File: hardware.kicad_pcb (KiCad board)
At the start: 2 copper layers, 25 x 31 mm, 11 parts, among them J2 MDT320B03001, P1 USB_C_Plug, U4 CH340C

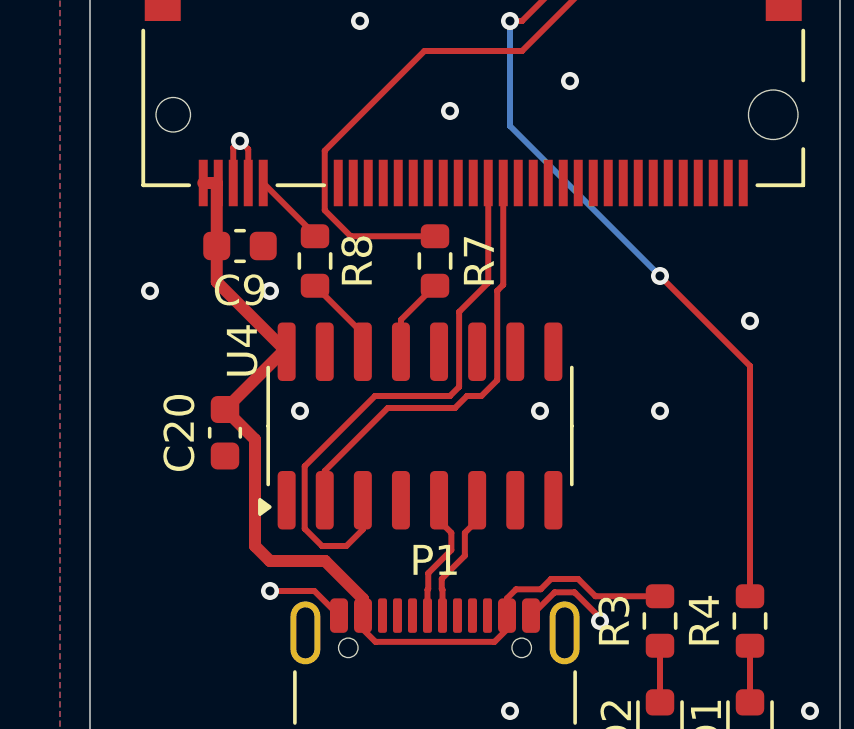
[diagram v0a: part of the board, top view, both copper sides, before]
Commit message: switch uart wiring
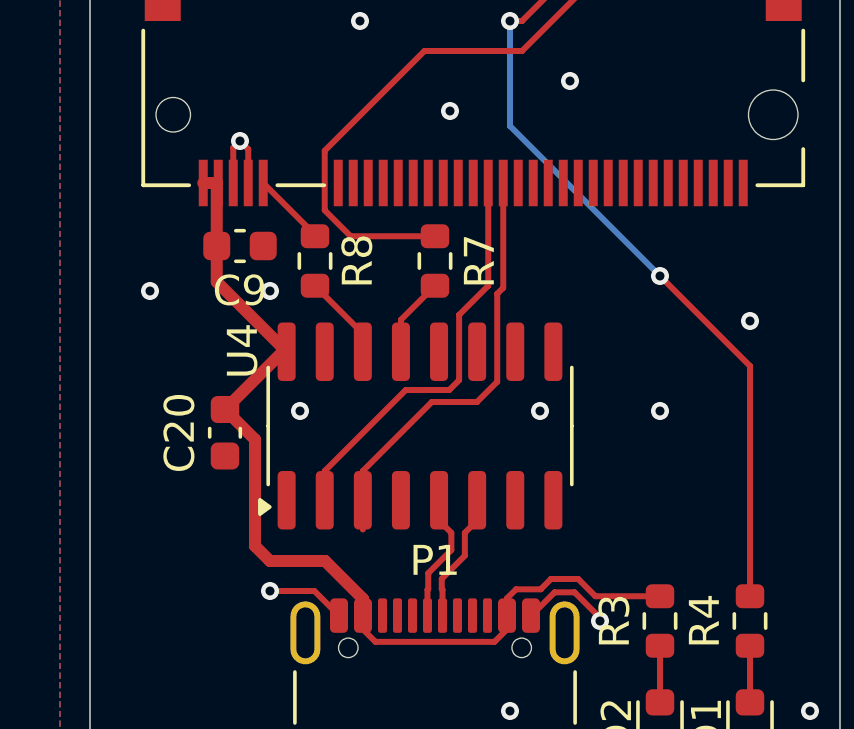
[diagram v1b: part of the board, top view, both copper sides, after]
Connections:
- U4 pad 2: IO4 -> IO5
- U4 pad 3: IO5 -> IO4
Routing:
- net IO5: track 18.9 -> 13.7 mm
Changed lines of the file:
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@@
 			(layers "F.Cu" "F.Mask" "F.Paste")
 			(roundrect_rratio 0.25)
-			(net 13 "IO4")
+			(net 5 "IO5")
 			(pinfunction "TXD")
 			(pintype "output")
@@
 			(layers "F.Cu" "F.Mask" "F.Paste")
 			(roundrect_rratio 0.25)
-			(net 5 "IO5")
+			(net 13 "IO4")
 			(pinfunction "RXD")
 			(pintype "input")
@@
 	)
 	(segment
-		(start 98.095 66.949999)
-		(end 97.544999 67.5)
-		(width 0.2)
-		(layer "F.Cu")
-		(net 5)
-	)
-	(segment
-		(start 98.5 62.5)
-		(end 101 62.5)
-		(width 0.2)
-		(layer "F.Cu")
-		(net 5)
-	)
-	(segment
-		(start 96.733032 67.5)
-		(end 96.156 66.922968)
-		(width 0.2)
-		(layer "F.Cu")
-		(net 5)
+		(start 100.228315 62.301)
+		(end 100.229316 62.3)
+		(width 0.2)
+		(layer "F.Cu")
+		(net 5)
+	)
+	(segment
+		(start 100.976968 62.3)
+		(end 101.304 61.972968)
+		(width 0.2)
+		(layer "F.Cu")
+		(net 5)
+	)
+	(segment
+		(start 96.825 65.000001)
+		(end 99.524001 62.301)
+		(width 0.2)
+		(layer "F.Cu")
+		(net 5)
+	)
+	(segment
+		(start 101.304 61.972968)
+		(end 101.304 59.796)
+		(width 0.2)
+		(layer "F.Cu")
+		(net 5)
+	)
+	(segment
+		(start 101.304 59.796)
+		(end 102.275 58.825)
+		(width 0.2)
+		(layer "F.Cu")
+		(net 5)
+	)
+	(segment
+		(start 96.825 65.975)
+		(end 96.825 65.000001)
+		(width 0.2)
+		(layer "F.Cu")
+		(net 5)
+	)
+	(segment
+		(start 100.229316 62.3)
+		(end 100.976968 62.3)
+		(width 0.2)
+		(layer "F.Cu")
+		(net 5)
+	)
+	(segment
+		(start 102.275 58.825)
+		(end 102.275 55.4)
+		(width 0.2)
+		(layer "F.Cu")
+		(net 5)
+	)
+	(segment
+		(start 99.524001 62.301)
+		(end 100.228315 62.301)
+		(width 0.2)
+		(layer "F.Cu")
+		(net 5)
+	)
+	(segment
+		(start 102.574 59.0931)
+		(end 102.775 58.8921)
+		(width 0.2)
+		(layer "F.Cu")
+		(net 13)
 	)
 	(segment
@@
 		(width 0.2)
 		(layer "F.Cu")
-		(net 5)
-	)
-	(segment
-		(start 97.544999 67.5)
-		(end 96.733032 67.5)
-		(width 0.2)
-		(layer "F.Cu")
-		(net 5)
-	)
-	(segment
-		(start 96.156 64.844)
-		(end 98.5 62.5)
-		(width 0.2)
-		(layer "F.Cu")
-		(net 5)
-	)
-	(segment
-		(start 101.304 59.696)
-		(end 102.275 58.725)
-		(width 0.2)
-		(layer "F.Cu")
-		(net 5)
-	)
-	(segment
-		(start 101 62.5)
-		(end 101.304 62.196)
-		(width 0.2)
-		(layer "F.Cu")
-		(net 5)
-	)
-	(segment
-		(start 101.304 62.196)
-		(end 101.304 59.696)
-		(width 0.2)
-		(layer "F.Cu")
-		(net 5)
-	)
-	(segment
-		(start 96.156 66.922968)
-		(end 96.156 64.844)
-		(width 0.2)
-		(layer "F.Cu")
-		(net 5)
-	)
-	(segment
-		(start 102.275 58.725)
-		(end 102.275 55.4)
-		(width 0.2)
-		(layer "F.Cu")
-		(net 5)
-	)
-	(segment
-		(start 101.565685 62.5)
-		(end 102.046968 62.5)
-		(width 0.2)
-		(layer "F.Cu")
-		(net 13)
-	)
-	(segment
-		(start 102.574 58.991686)
-		(end 102.775 58.790686)
-		(width 0.2)
-		(layer "F.Cu")
-		(net 13)
-	)
-	(segment
-		(start 102.046968 62.5)
-		(end 102.574 61.972968)
-		(width 0.2)
-		(layer "F.Cu")
-		(net 13)
-	)
-	(segment
-		(start 96.825 65.975)
-		(end 96.825 65.000001)
-		(width 0.2)
-		(layer "F.Cu")
-		(net 13)
-	)
-	(segment
-		(start 96.825 65.000001)
-		(end 98.925001 62.9)
-		(width 0.2)
-		(layer "F.Cu")
-		(net 13)
-	)
-	(segment
-		(start 102.574 61.972968)
-		(end 102.574 58.991686)
-		(width 0.2)
-		(layer "F.Cu")
-		(net 13)
-	)
-	(segment
-		(start 101.165685 62.9)
-		(end 101.565685 62.5)
-		(width 0.2)
-		(layer "F.Cu")
-		(net 13)
-	)
-	(segment
-		(start 102.775 58.790686)
+		(net 13)
+	)
+	(segment
+		(start 98.095 65.975)
+		(end 98.095 65.000001)
+		(width 0.2)
+		(layer "F.Cu")
+		(net 13)
+	)
+	(segment
+		(start 100.395001 62.7)
+		(end 101.9 62.7)
+		(width 0.2)
+		(layer "F.Cu")
+		(net 13)
+	)
+	(segment
+		(start 101.9 62.7)
+		(end 102.574 62.026)
+		(width 0.2)
+		(layer "F.Cu")
+		(net 13)
+	)
+	(segment
+		(start 98.095 65.000001)
+		(end 100.395001 62.7)
+		(width 0.2)
+		(layer "F.Cu")
+		(net 13)
+	)
+	(segment
+		(start 102.574 62.026)
+		(end 102.574 59.0931)
+		(width 0.2)
+		(layer "F.Cu")
+		(net 13)
+	)
+	(segment
+		(start 102.775 58.8921)
 		(end 102.775 55.4)
 		(width 0.2)
 		(layer "F.Cu")
-		(net 13)
-	)
-	(segment
-		(start 98.925001 62.9)
-		(end 101.165685 62.9)
-		(width 0.2)
-		(layer "F.Cu")

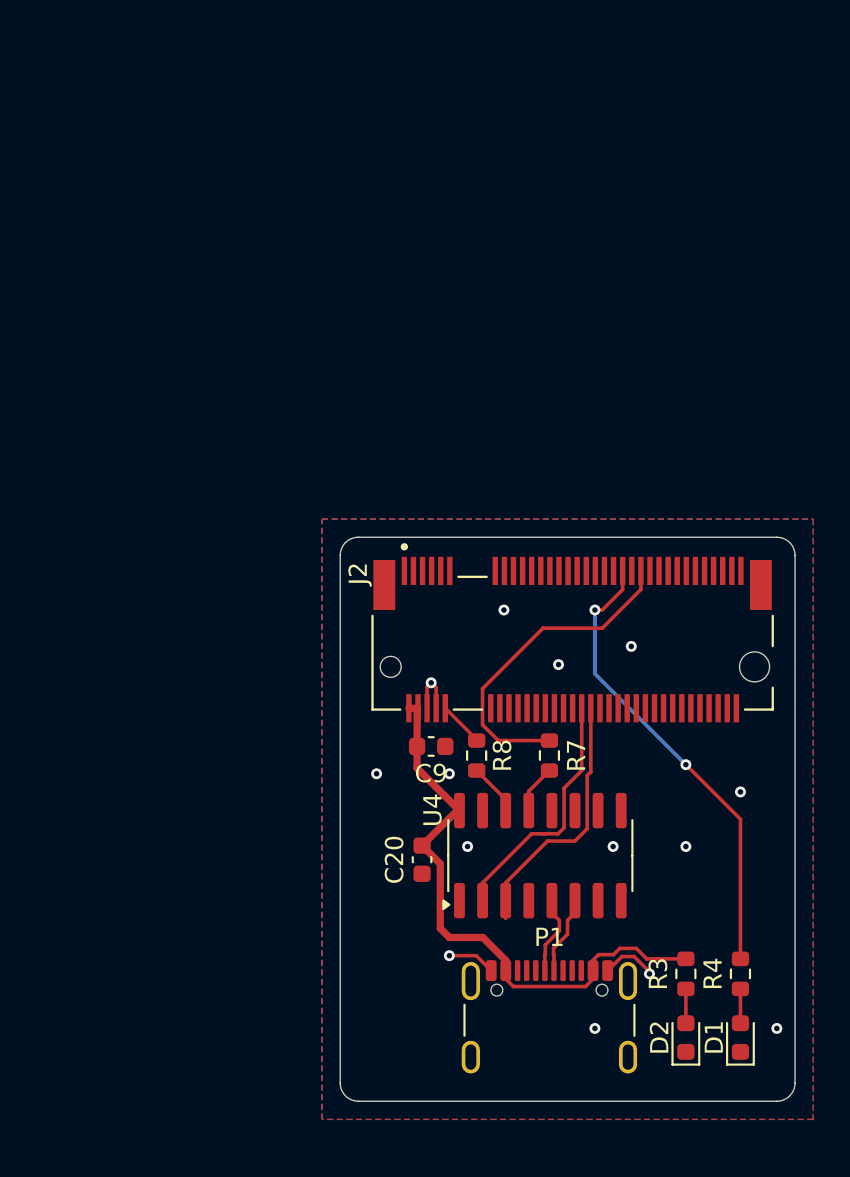
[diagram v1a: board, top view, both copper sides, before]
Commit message: add testing header
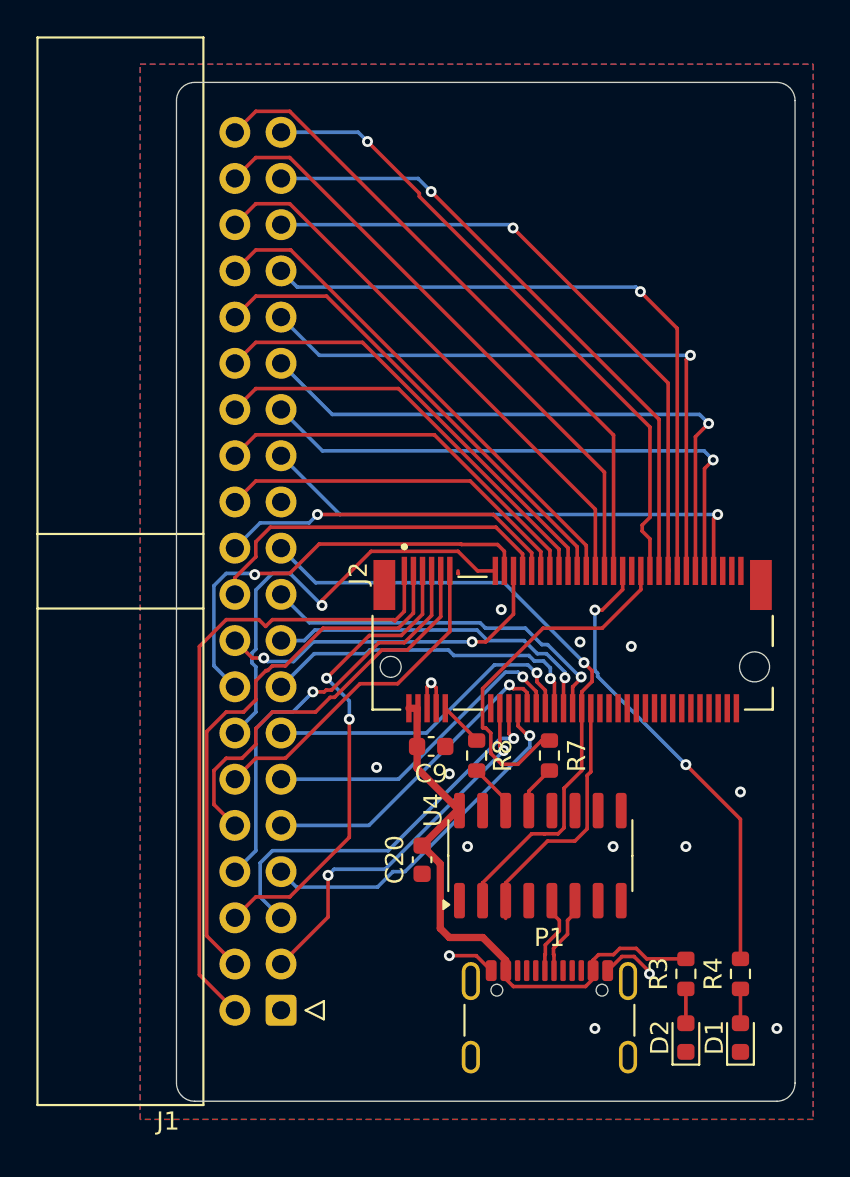
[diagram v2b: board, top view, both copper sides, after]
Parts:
- added J1: Conn_02x20_Odd_Even, Connector_IDC:IDC-Header_2x20_P2.54mm_Horizontal, F.Cu at (85.8, 72.0)
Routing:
- net IO12: track 0.00 -> 36.4 mm, vias 0 -> 1
- net IO21: track 0.00 -> 36.1 mm
- net IO39: track 0.00 -> 35.5 mm
- net IO15: track 0.00 -> 35.4 mm, vias 0 -> 1
- net IO17: track 0.00 -> 35.3 mm, vias 0 -> 1
- net IO13: track 0.00 -> 35.3 mm, vias 0 -> 1
- net IO14: track 0.00 -> 34.6 mm, vias 0 -> 1
- net IO20: track 0.00 -> 33.4 mm
- net IO10: track 0.00 -> 33.3 mm, vias 0 -> 1
- net IO11: track 0.00 -> 31.2 mm, vias 0 -> 1
- net IO23: track 0.00 -> 30.6 mm
- net IO37: track 0.00 -> 30.4 mm
- net IO9: track 0.00 -> 28.5 mm, vias 0 -> 1
- net IO22: track 0.00 -> 27.9 mm
- net IO38: track 0.00 -> 26.5 mm, vias 0 -> 2
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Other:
- board size 25 x 31 mm -> 34 x 56 mm

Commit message: add rst/boot pull up
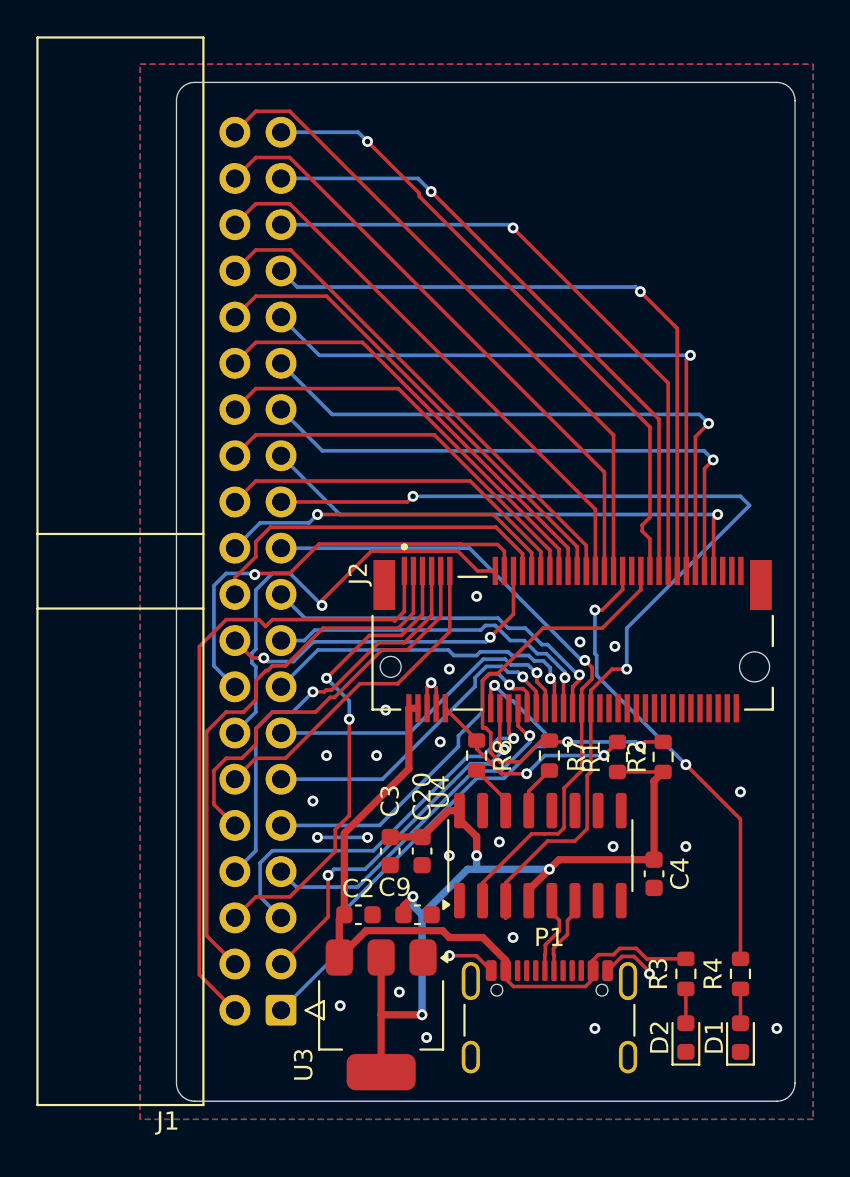
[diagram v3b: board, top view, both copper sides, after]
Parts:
- added C2: C, Capacitor_SMD:C_0603_1608Metric, F.Cu at (90.0, 66.8)
- added C3: C, Capacitor_SMD:C_0603_1608Metric, F.Cu at (91.8, 63.2)
- added C4: C, Capacitor_SMD:C_0603_1608Metric, F.Cu at (106.2, 64.5)
- added R1: 1.1K, Resistor_SMD:R_0603_1608Metric, F.Cu at (104.2, 58.1)
- added R2: 1.1K, Resistor_SMD:R_0603_1608Metric, F.Cu at (106.8, 58.1)
- added U3: AMS1117-3.3, Package_TO_SOT_SMD:SOT-223-3_TabPin2, F.Cu at (91.2, 72.2)
- moved C9 9.28 mm to (93.2, 66.8)
- moved C20 0.48 mm to (93.5, 63.2)
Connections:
- C20 pad 1: +5V -> +3V3
- C9 pad 1: +5V -> +3V3
- U4 pad 16: +5V -> +3V3
- U4 pad 4: unconnected-(U4-V3-Pad4) -> +3V3
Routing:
- net +3V3: track 0.00 -> 48.2 mm, vias 0 -> 4
- net IO4: track 14.4 -> 55.7 mm, vias 0 -> 2
- net IO47: track 0.00 -> 27.6 mm, vias 0 -> 1
- net RST: track 2.49 -> 12.0 mm, vias 0 -> 2
- net +5V: track 32.0 -> 39.0 mm
- net BOOT: track 19.8 -> 26.5 mm, vias 0 -> 2
- net GND: track 8.73 -> 11.5 mm, vias 14 -> 25
- net IO40: track 17.8 -> 19.6 mm
- net IO42: track 17.9 -> 18.4 mm

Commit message: fix usb c wiring
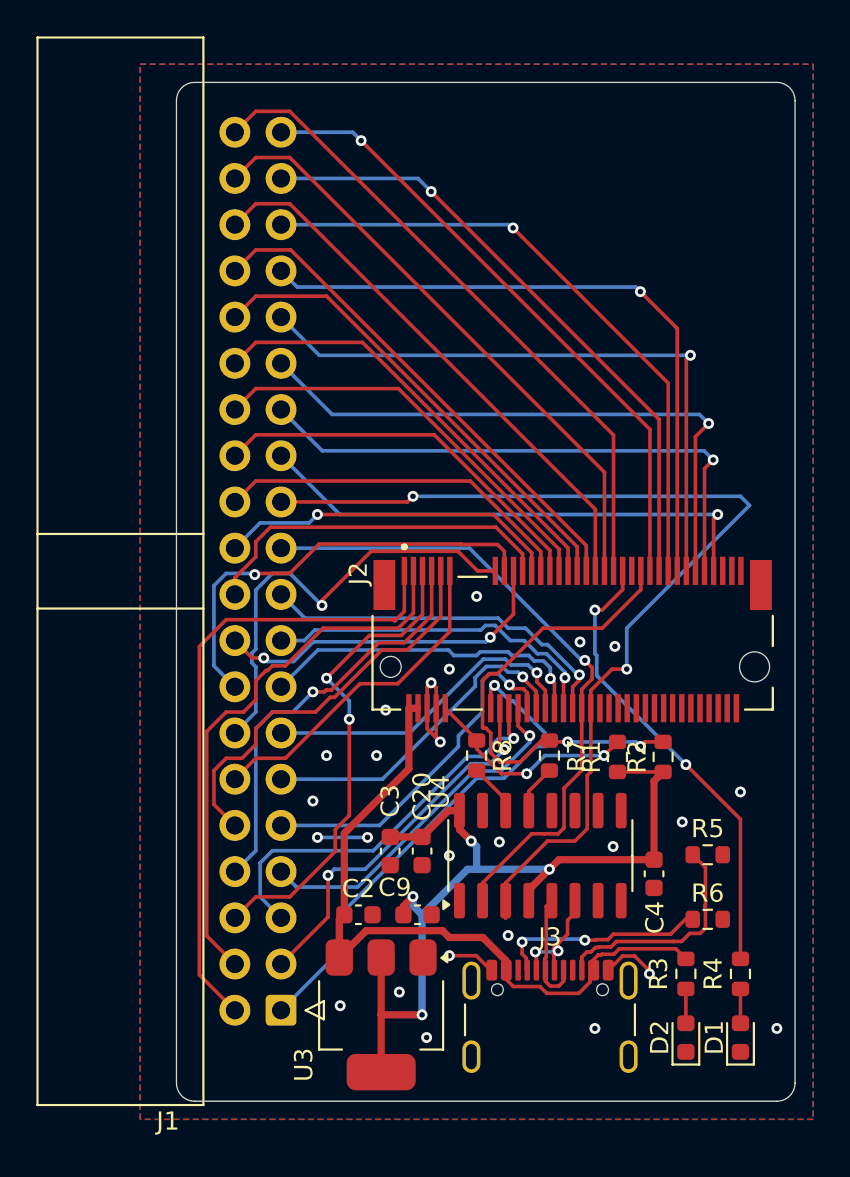
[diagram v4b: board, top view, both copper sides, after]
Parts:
- removed P1: USB_C_Plug, Connector_USB:USB_C_Receptacle_GCT_USB4105-xx-A_16P_TopMnt_Horizontal
- added J3: USB_C_Receptacle_USB2.0_16P, Connector_USB:USB_C_Receptacle_GCT_USB4105-xx-A_16P_TopMnt_Horizontal, F.Cu at (100.5, 73.5)
- added R5: 5.1K, Resistor_SMD:R_0603_1608Metric, F.Cu at (109.2, 63.5)
- added R6: 5.1K, Resistor_SMD:R_0603_1608Metric, F.Cu at (109.2, 67.0)
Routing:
- net Net-(J3-CC2): track 0.00 -> 12.5 mm
- net Net-(J3-CC1): track 0.00 -> 11.6 mm, vias 0 -> 2
- net GND: track 11.5 -> 15.6 mm
- net D-: track 4.34 -> 7.01 mm, vias 0 -> 2
- net D+: track 4.34 -> 6.44 mm
- net IO17: track 35.3 -> 34.8 mm
